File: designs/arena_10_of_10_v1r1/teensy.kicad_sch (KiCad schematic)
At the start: 37 parts, among them J1 Cetus RJ45 Magjack, J2 Conn_01x02, J3 Conn_Coaxial, J4 Conn_Coaxial, U1 Teensy4.1, U2 SN74LV1T34DBV, U3 SN74LV1T34DBV

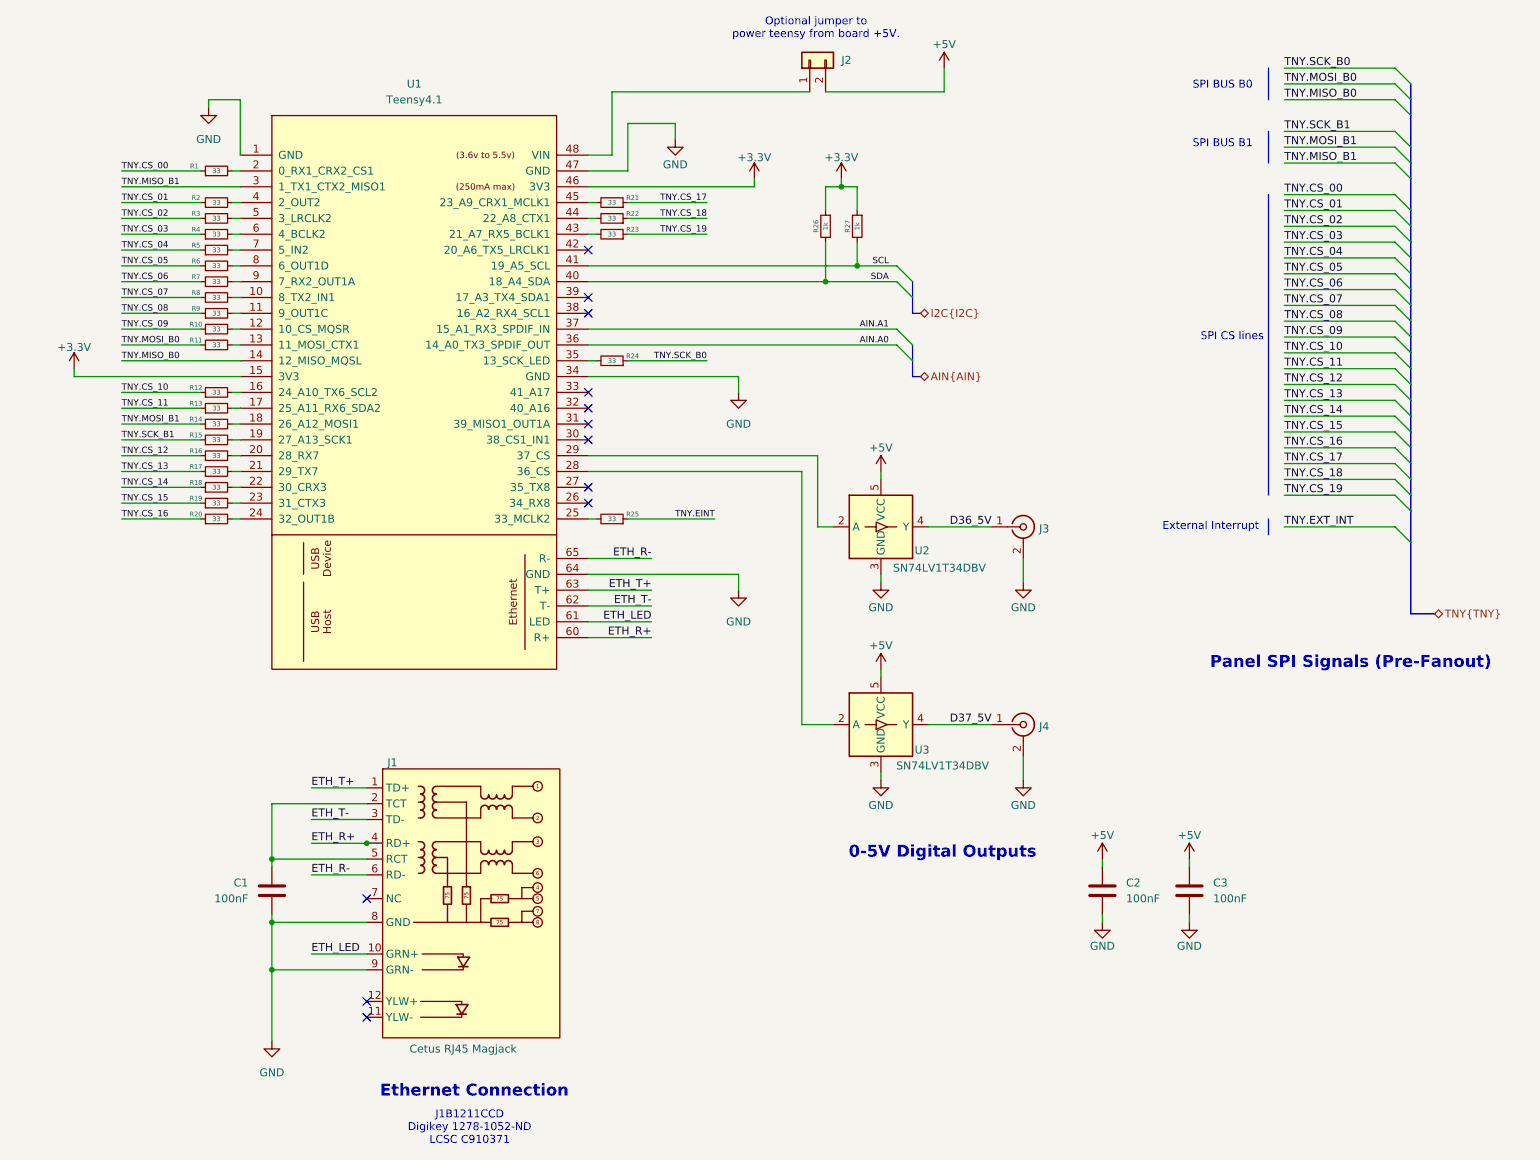
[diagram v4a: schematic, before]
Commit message: Working through schematic design rule check.
Just some power issues remaing.
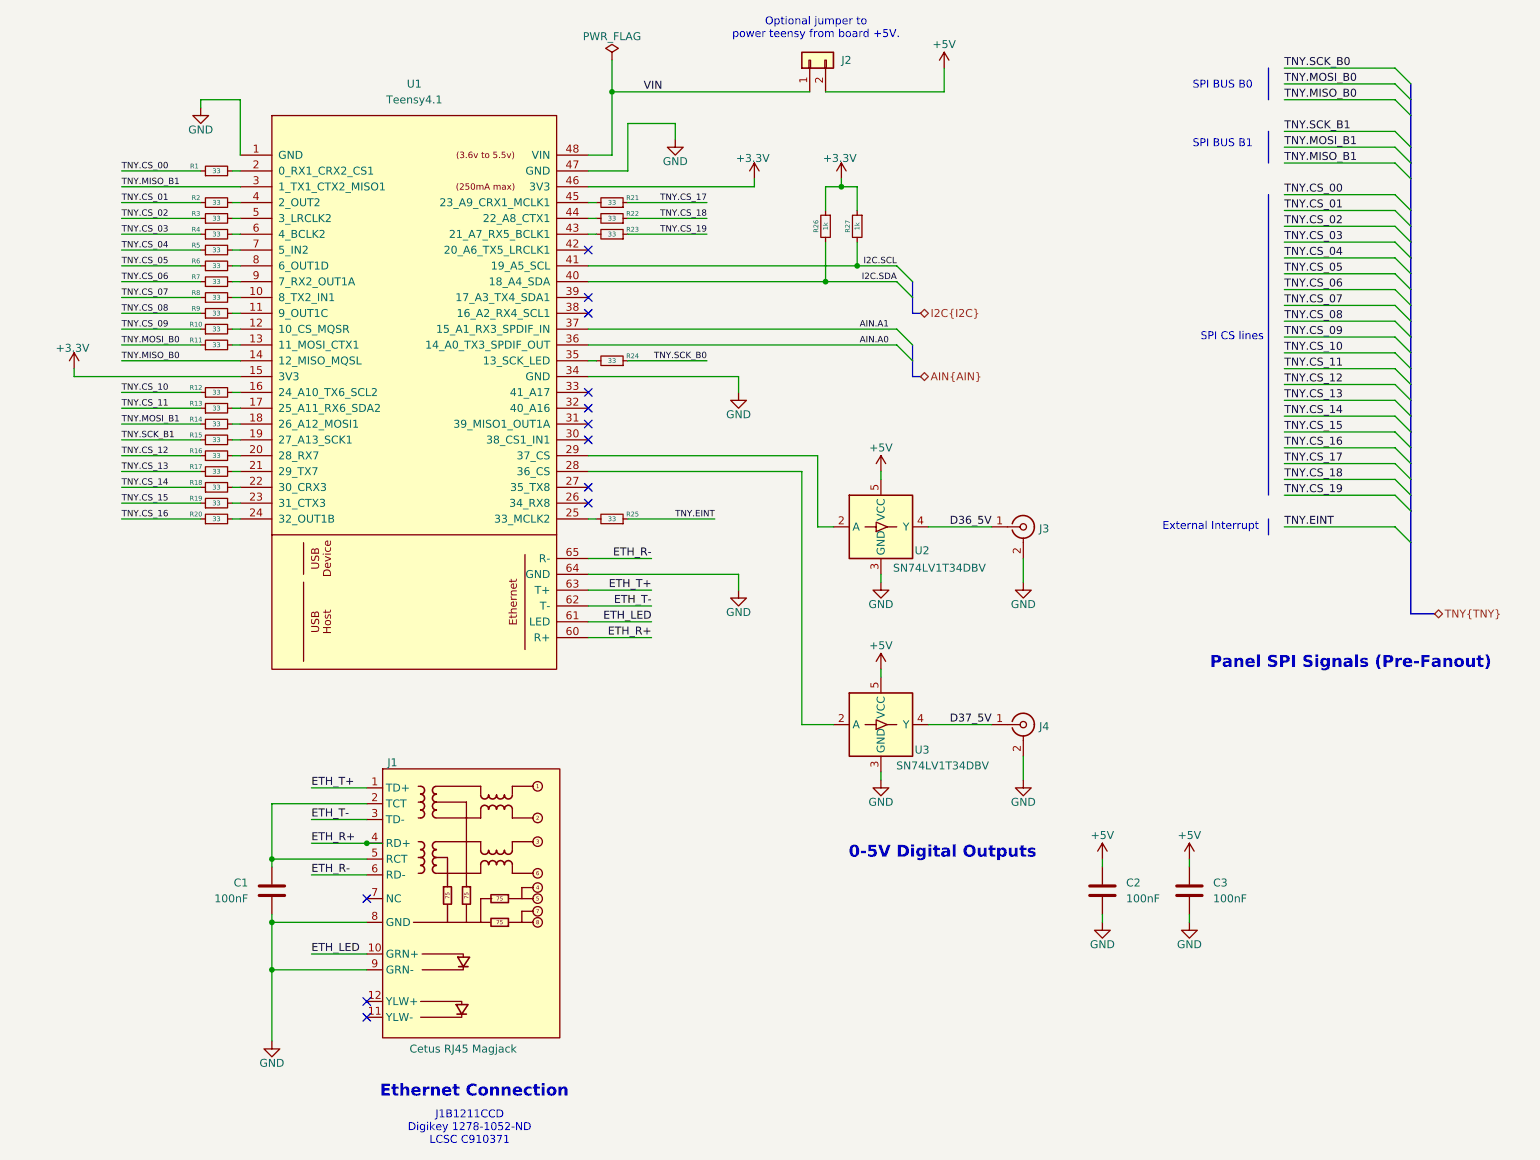
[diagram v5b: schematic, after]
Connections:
- net VIN: now reaches J2.1 (Pin_1), U1.48 (VIN)
- net SCL renamed I2C.SCL
- net SDA renamed I2C.SDA

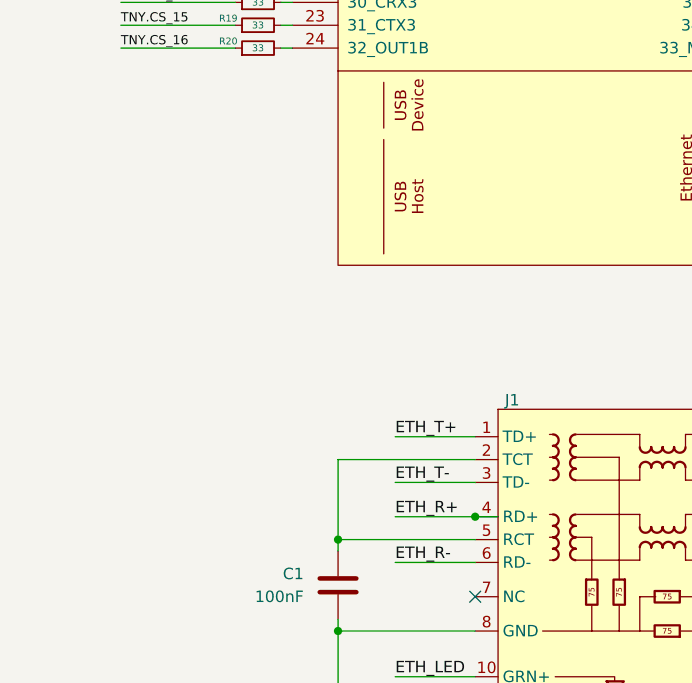
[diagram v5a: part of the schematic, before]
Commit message: Resolved all DSR voilations in schematic.
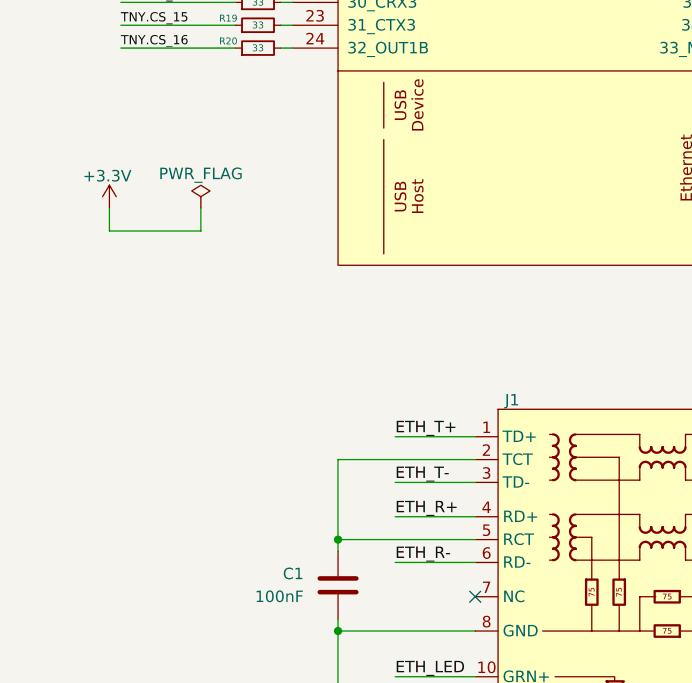
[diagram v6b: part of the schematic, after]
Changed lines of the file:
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@@
 	)
 	(junction
-		(at 69.85 148.59)
-		(diameter 0)
-		(color 0 0 0 0)
-	)
-	(junction
 		(at 109.22 27.94)
 		(diameter 0)
@@
 	(wire
 		(pts
+			(xy 39.37 116.84) (xy 39.37 114.3)
+		)
+		(stroke
+			(width 0)
+			(type default)
+		)
+	)
+	(wire
+		(pts
 			(xy 160.02 97.79) (xy 170.18 97.79)
 		)
@@
 	(wire
 		(pts
+			(xy 29.21 114.3) (xy 29.21 116.84)
+		)
+		(stroke
+			(width 0)
+			(type default)
+		)
+	)
+	(wire
+		(pts
 			(xy 234.95 57.15) (xy 217.17 57.15)
 		)
@@
 		)
 	)
+	(wire
+		(pts
+			(xy 29.21 116.84) (xy 39.37 116.84)
+		)
+		(stroke
+			(width 0)
+			(type default)
+		)
+	)
 	(polyline
 		(pts
@@
 	(wire
 		(pts
+			(xy 60.96 148.59) (xy 69.85 148.59)
+		)
+		(stroke
+			(width 0)
+			(type default)
+		)
+	)
+	(wire
+		(pts
 			(xy 234.95 69.85) (xy 217.17 69.85)
 		)
@@
 		)
 	)
-	(wire
-		(pts
-			(xy 60.96 148.59) (xy 69.85 148.59)
-		)
-		(stroke
-			(width 0)
-			(type default)
-		)
-	)
 	(bus
 		(pts
@@
 	(wire
 		(pts
-			(xy 72.39 148.59) (xy 69.85 148.59)
-		)
-		(stroke
-			(width 0)
-			(type default)
-		)
-	)
-	(wire
-		(pts
 			(xy 143.51 27.94) (xy 162.56 27.94)
 		)
@@
 	)
 	(symbol
+		(lib_id "power:+5V")
+		(at 152.4 88.9 0)
+		(unit 1)
+		(exclude_from_sim no)
+		(in_bom yes)
+		(on_board yes)
+		(dnp no)
+		(property "Reference" "#PWR09"
+			(at 152.4 92.71 0)
+			(effects
+				(font
+					(size 1.27 1.27)
+				)
+				(hide yes)
+			)
+		)
+		(property "Value" "+5V"
+			(at 152.4 85.09 0)
+			(effects
+				(font
+					(size 1.27 1.27)
+				)
+			)
+		)
+		(property "Footprint" ""
+			(at 152.4 88.9 0)
+			(effects
+				(font
+					(size 1.27 1.27)
+				)
+				(hide yes)
+			)
+		)
+		(property "Datasheet" ""
+			(at 152.4 88.9 0)
+			(effects
+				(font
+					(size 1.27 1.27)
+				)
+				(hide yes)
+			)
+		)
+		(property "Description" "Power symbol creates a global label with name \"+5V\""
+			(at 152.4 88.9 0)
+			(effects
+				(font
+					(size 1.27 1.27)
+				)
+				(hide yes)
+			)
+		)
+		(pin "1"
+		)
+		(instances
+			(project "arena_10_of_10_v1r1"
+				(path "/056666d2-2c8f-491c-bcad-db3c517779a8/49d7122d-250d-4ac4-9432-46d5d4ec4ae4"
+					(reference "#PWR09")
+					(unit 1)
+				)
+			)
+		)
+	)
+	(symbol
 		(lib_id "Device:R_Small")
 		(at 45.72 45.72 90)
@@
 	)
 	(symbol
+		(lib_id "power:+3.3V")
+		(at 29.21 114.3 0)
+		(unit 1)
+		(exclude_from_sim no)
+		(in_bom yes)
+		(on_board yes)
+		(dnp no)
+		(property "Reference" "#PWR0263"
+			(at 29.21 118.11 0)
+			(effects
+				(font
+					(size 1.27 1.27)
+				)
+				(hide yes)
+			)
+		)
+		(property "Value" "+3.3V"
+			(at 28.956 110.744 0)
+			(effects
+				(font
+					(size 1.27 1.27)
+				)
+			)
+		)
+		(property "Footprint" ""
+			(at 29.21 114.3 0)
+			(effects
+				(font
+					(size 1.27 1.27)
+				)
+				(hide yes)
+			)
+		)
+		(property "Datasheet" ""
+			(at 29.21 114.3 0)
+			(effects
+				(font
+					(size 1.27 1.27)
+				)
+				(hide yes)
+			)
+		)
+		(property "Description" "Power symbol creates a global label with name \"+3.3V\""
+			(at 29.21 114.3 0)
+			(effects
+				(font
+					(size 1.27 1.27)
+				)
+				(hide yes)
+			)
+		)
+		(pin "1"
+		)
+		(instances
+			(project "arena_10_of_10_v1r1"
+				(path "/056666d2-2c8f-491c-bcad-db3c517779a8/49d7122d-250d-4ac4-9432-46d5d4ec4ae4"
+					(reference "#PWR0263")
+					(unit 1)
+				)
+			)
+		)
+	)
+	(symbol
 		(lib_id "Device:R_Small")
 		(at 45.72 93.98 90)
@@
 	)
 	(symbol
-		(lib_id "power:+5V")
-		(at 152.4 88.9 0)
+		(lib_id "power:PWR_FLAG")
+		(at 39.37 114.3 0)
 		(unit 1)
 		(exclude_from_sim no)
@@
 		(on_board yes)
 		(dnp no)
-		(property "Reference" "#PWR09"
-			(at 152.4 92.71 0)
+		(property "Reference" "#FLG01"
+			(at 39.37 112.395 0)
 			(effects
 				(font
@@
 			)
 		)
-		(property "Value" "+5V"
-			(at 152.4 85.09 0)
+		(property "Value" "PWR_FLAG"
+			(at 39.37 110.49 0)
 			(effects
 				(font
@@
 		)
 		(property "Footprint" ""
-			(at 152.4 88.9 0)
+			(at 39.37 114.3 0)
 			(effects
 				(font
@@
 			)
 		)
-		(property "Datasheet" ""
-			(at 152.4 88.9 0)
+		(property "Datasheet" "~"
+			(at 39.37 114.3 0)
 			(effects
 				(font
@@
 			)
 		)
-		(property "Description" "Power symbol creates a global label with name \"+5V\""
-			(at 152.4 88.9 0)
+		(property "Description" "Special symbol for telling ERC where power comes from"
+			(at 39.37 114.3 0)
 			(effects
 				(font
@@
 			(project "arena_10_of_10_v1r1"
 				(path "/056666d2-2c8f-491c-bcad-db3c517779a8/49d7122d-250d-4ac4-9432-46d5d4ec4ae4"
-					(reference "#PWR09")
+					(reference "#FLG01")
 					(unit 1)
 				)
